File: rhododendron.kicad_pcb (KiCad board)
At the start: 2 copper layers, 70.7 x 53.3 mm, 42 parts, among them J1 Conn_02x20_Odd_Even, J2 Conn_02x20_Odd_Even, J4 USB-A-SHIELDED, J5 USB-B-SHIELDED, J7 BONUS_ROW, U1 USB3343, Y1 26MHz

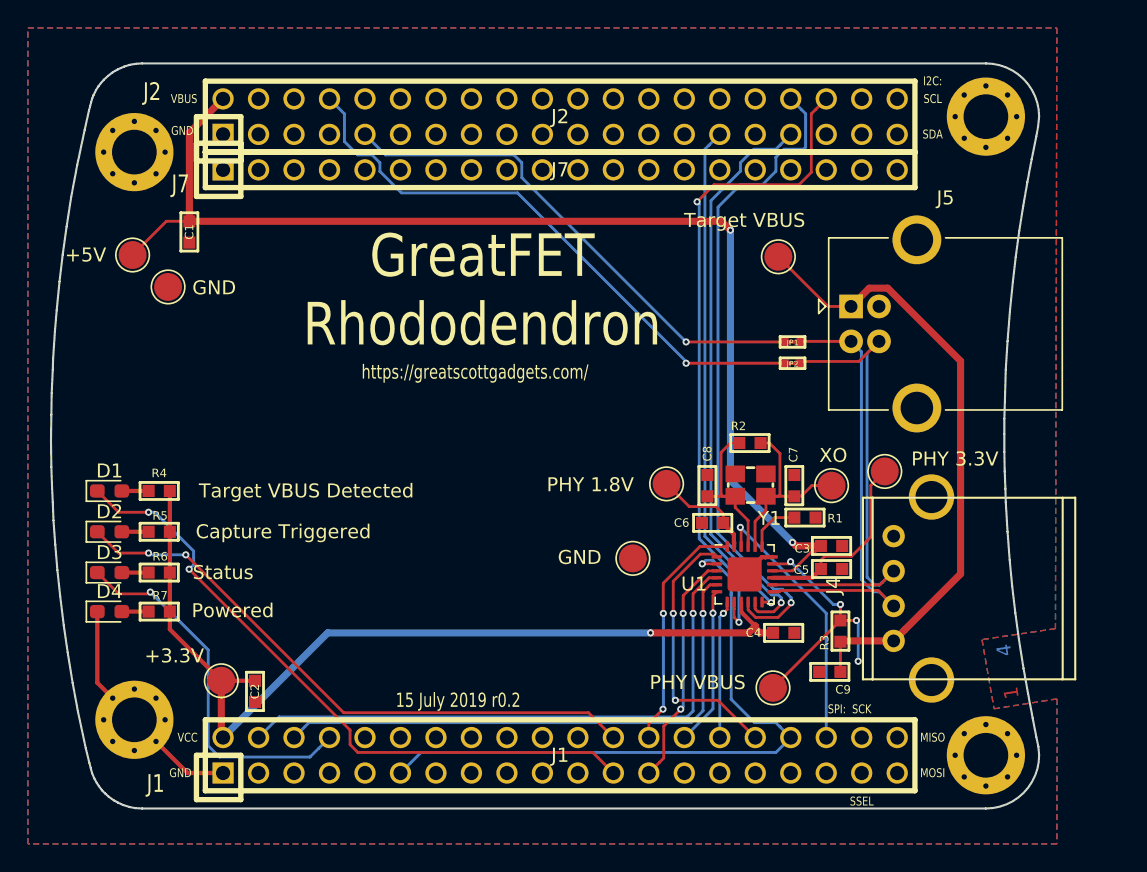
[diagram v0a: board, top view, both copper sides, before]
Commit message: r0.2: finalize for ordering; improve silkscreen; minor tweaks
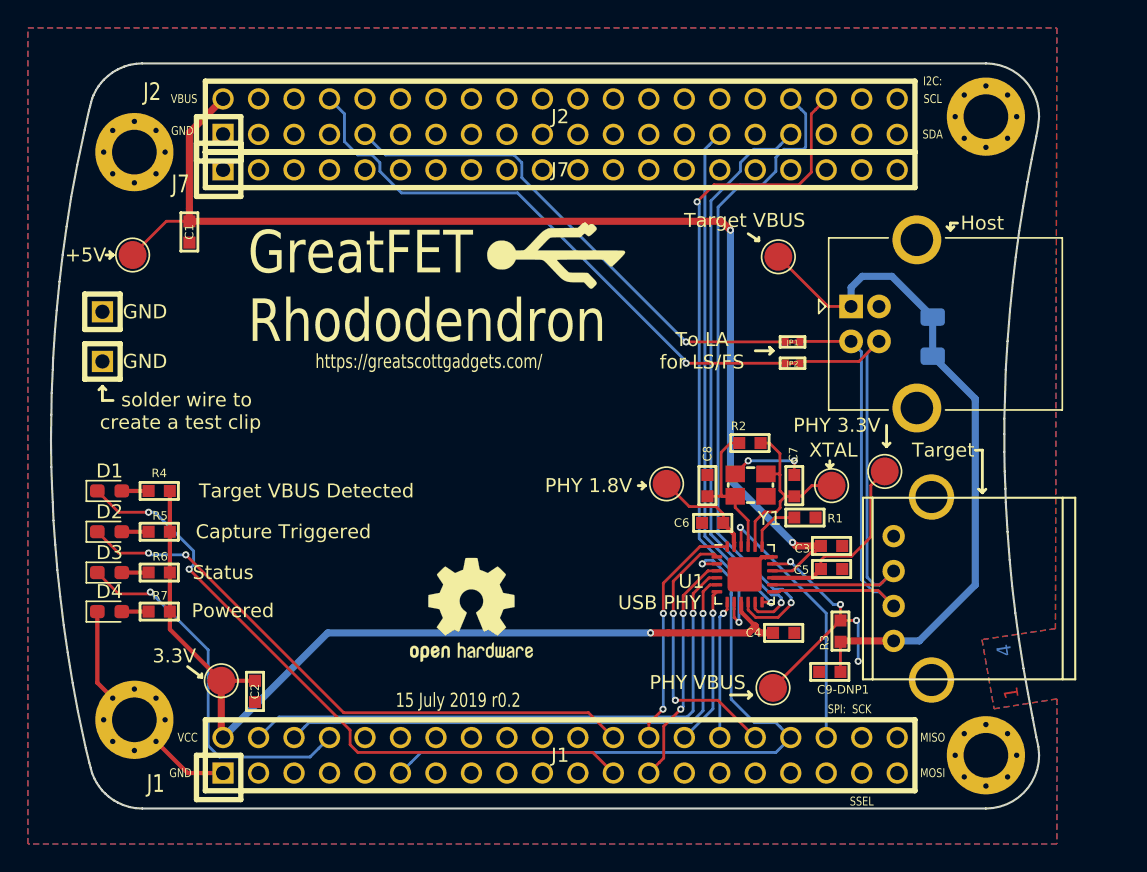
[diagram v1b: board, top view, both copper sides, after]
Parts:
- removed the GND at (118.0, 84.6)
- removed the GND at (151.3, 104.0)
- removed J4: USB-A-SHIELDED, rhododendron:CONN-Amphenol-UE27AC54100
- removed J5: USB-B-SHIELDED, rhododendron:USB_B_OST_USB-B1HSxx_Horizontal
- added G***: LOGO, rhododendron:usb_tools_logo, F.Cu at (145.8, 82.3)
- added G***: LOGO, rhododendron:usb_tools_logo, F.Cu at (142.2, 105.4)
- added GND: TestPoint, gsg-modules:HEADER-1x1, F.Cu at (113.3, 89.9)
- added GND: TestPoint, gsg-modules:HEADER-1x1, F.Cu at (113.3, 86.4)
- added Host: USB-B-SHIELDED, rhododendron:USB_B_OST_USB-B1HSxx_Horizontal, F.Cu at (166.9, 86.0)
- added R8: DNP, Resistor_SMD:R_1206_3216Metric, B.Cu at (172.7, 88.1)
- added REF**: OSHW-Logo2_9.8x8mm_SilkScreen, Symbol:OSHW-Logo2_9.8x8mm_SilkScreen, F.Cu at (139.7, 107.7)
- added Target: USB-A-SHIELDED, rhododendron:CONN-Amphenol-UE27AC54100, F.Cu at (169.9, 106.2)
- renumbered +3.3V to 3.3V, C9 to C9-DNP1, XO to XTAL
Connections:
- net /PHY_26MHZ_IN renamed /PHY_XI
- Y1 pad 2: /PHY_XO -> GND
- Y1 pad 3: (no net) -> /PHY_XO
- Y1 pad 4: (no net) -> GND
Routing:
- net GND: track 19.3 -> 25.8 mm, vias 0 -> 2
- net /TARGET_VBUS: track 45.2 -> 49.4 mm
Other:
- board text added: "To LA for LS/FS"
- board text added: "USB PHY"
- board text added: "cut trace to separate VBUSes or add a current-sense resistor"
- board text added: "solder wire to create a test clip"

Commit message: r0.3: route the changes made in the r0.3 schematic
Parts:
- removed C8: 8.2pF, gsg-modules:0603
- removed PHY VBUS: TestPoint, TestPoint:TestPoint_Pad_D2.0mm
- removed XTAL: TestPoint, TestPoint:TestPoint_Pad_D2.0mm
- removed Y1: 26MHz, gsg-modules:XTAL3.2x2.5mm
- added D5: LED, LED_SMD:LED_0603_1608Metric_Pad1.05x0.95mm_HandSolder, F.Cu at (113.7, 108.5)
- added JP3: Jumper_NC_Small, gsg-modules:0402-SHORT-10MIL, F.Cu at (146.6, 83.9)
- added R10: 1K, gsg-modules:0603, F.Cu at (162.7, 90.0)
- added R12: 1K, gsg-modules:0603, F.Cu at (165.1, 79.6)
- added R13: 1K5, gsg-modules:0603, F.Cu at (168.3, 79.6)
- added R14: 10K, gsg-modules:0603, F.Cu at (167.3, 114.3)
- added R9: 1K, gsg-modules:0603, F.Cu at (162.7, 88.5)
- added TP4: TestPoint, TestPoint:TestPoint_Pad_D2.0mm, F.Cu at (156.6, 97.0)
- added TP6: TestPoint, TestPoint:TestPoint_Pad_D2.0mm, F.Cu at (161.3, 113.3)
- added TP7: TestPoint, TestPoint:TestPoint_Pad_D2.0mm, F.Cu at (141.6, 82.3)
- added U2: M24C02-FMN, Package_SO:SOIC-8_3.9x4.9mm_P1.27mm, F.Cu at (151.5, 83.3)
- C7: value 8.2pF -> 10nF
- R2: value 1M -> 330
- TP1: renamed from PHY 3.3V
- TP5: renamed from PHY 1.8V
- TP8: renamed from Target VBUS
- moved R2 44.3 mm to (117.2, 108.5), turned to 0 degrees
- moved JP2 17.7 mm to (146.6, 82.7)
- moved JP1 17.7 mm to (146.5, 81.4)
- moved C7 16.6 mm to (151.3, 86.9), turned to 0 degrees
- moved G*** 10.4 mm to (151.1, 91.2)
- moved TP1 3.51 mm to (165.9, 98.6)
- moved REF** 2.96 mm to (140.2, 104.8)
- moved D2 2.42 mm to (113.7, 99.7)
- moved R5 2.42 mm to (117.2, 99.7)
- moved D1 2.42 mm to (113.7, 96.8)
- moved D3 2.42 mm to (113.7, 102.6)
- moved D4 2.42 mm to (113.7, 105.4)
- moved R4 2.42 mm to (117.2, 96.8)
- moved R6 2.42 mm to (117.2, 102.6)
- moved R7 2.42 mm to (117.2, 105.4)
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- renumbered C9-DNP1 to C9, Target to Device, +5V to TP2, 3.3V to TP3, GND to TP9
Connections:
- net /LED_STATUS renamed /LED_CAPTURING
- C7 pad 2: /PHY_XO -> +3V3
- J1 pad 11: /ULPI_CLK -> +3V3
- J1 pad 14: /P5_2 -> /LED_ERROR
- J1 pad 16: /P1_6 -> /ULPI_DIR
- J1 pad 34: /ULPI_CLK -> +3V3
- J1 pad 35: /P2_0 -> /~PHY_RESET
- J1 pad 36: /~PHY_RESET -> /P6_3
- J1 pad 7: /P1_0 -> /ULPI_NXT
- J2 pad 12: /CLK2 -> /REFCLK
- J2 pad 18: /P2_5 -> /REFCLK
- J2 pad 20: /P2_3 -> /ULPI_DATA5
- J2 pad 23: /P7_2 -> /ULPI_DATA4
- J2 pad 37: /P3_5 -> /TARGET_VBUS_DETECT
- J2 pad 38: /P3_6 -> /I2C_EEPROM_WC
- J7 pad 10: GND -> /RTCX1
- J7 pad 20: VCC -> +3V3
- J7 pad 4: /ADC0_5 -> /PHY_VDD18
- JP1 pad 1: /LA_USB_D- -> GND
- JP1 pad 2: /USB_D- -> Net-(JP1-Pad2)
- JP2 pad 1: /LA_USB_D+ -> GND
- JP2 pad 2: /USB_D+ -> Net-(JP2-Pad2)
- R2 pad 1: /PHY_XO -> Net-(D5-Pad2)
- R2 pad 2: /PHY_XI -> +3V3
- U1 pad 2: /ULPI_CLK -> +3V3
- U1 pad 20: /PHY_XO -> Net-(U1-Pad20)
- U1 pad 21: /PHY_XI -> /REFCLK
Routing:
- net +3V3: track 66.8 -> 132.2 mm, vias 1 -> 11
- net /REFCLK: track 0.00 -> 53.3 mm, vias 0 -> 1
- net /ULPI_CLK: track 46.9 -> 0.00 mm, vias 1 -> 0
- net /PHY_VDD18: track 7.61 -> 49.7 mm, vias 0 -> 1
- net /LED_ERROR: track 0.00 -> 31.7 mm
- net /ULPI_NXT: track 16.9 -> 40.8 mm
- net /I2C0_SCL: track 0.00 -> 23.4 mm
- net /I2C0_SDA: track 0.00 -> 21.9 mm
- net /I2C_EEPROM_WC: track 0.00 -> 21.0 mm, vias 0 -> 1
- net /ULPI_DATA5: track 47.8 -> 66.7 mm
- net /ULPI_DIR: track 19.4 -> 36.2 mm
- net /ULPI_DATA4: track 47.8 -> 62.8 mm
- net /PHY_XO: track 14.6 -> 0.00 mm
- net /PHY_XI: track 11.6 -> 0.00 mm
- net GND: track 25.8 -> 16.0 mm
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- added copper zone on B.Cu, net +3V3
- removed copper zone on B.Cu, net VCC
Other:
- board size 70.7 x 53.3 mm -> 73.7 x 53.3 mm
- board text added: "16 October 2019 r0.3"
- board text added: "2"
- board text added: "3.3V"
- board text added: "5V"
- board text added: "Capture Active"
- board text added: "Error"
- board text added: "GND Clip"
- board text added: "High Speed USB Analyzer for GreatFET"
- board text added: "ID ROM"
- board text added: "PHY 1.8V"
- board text added: "PHY 3.3V"
- board text added: "PHY Clock"
- board text added: "PHY VBus"
- board text added: "Rhododendron"
- board text added: "VCCIO 3.3V"
- board text added: "design by Kate Temkin (@ktemkin); with help from Mikaela Szekely (@Qyriad)"
- board text removed: "15 July 2019 r0.2"
- board text removed: "4"
- board text removed: "GreatFET Rhododendron"
- board text removed: "MISO"
- board text removed: "MOSI"
- board text removed: "SCK"
- board text removed: "SPI:"
- board text removed: "SSEL"
- board text removed: "Status"
- board text removed: "To LA for LS/FS"
- board text removed: "design by @ktemkin; with help from @Qyriad"
- board text removed: "solder wire to create a test clip"

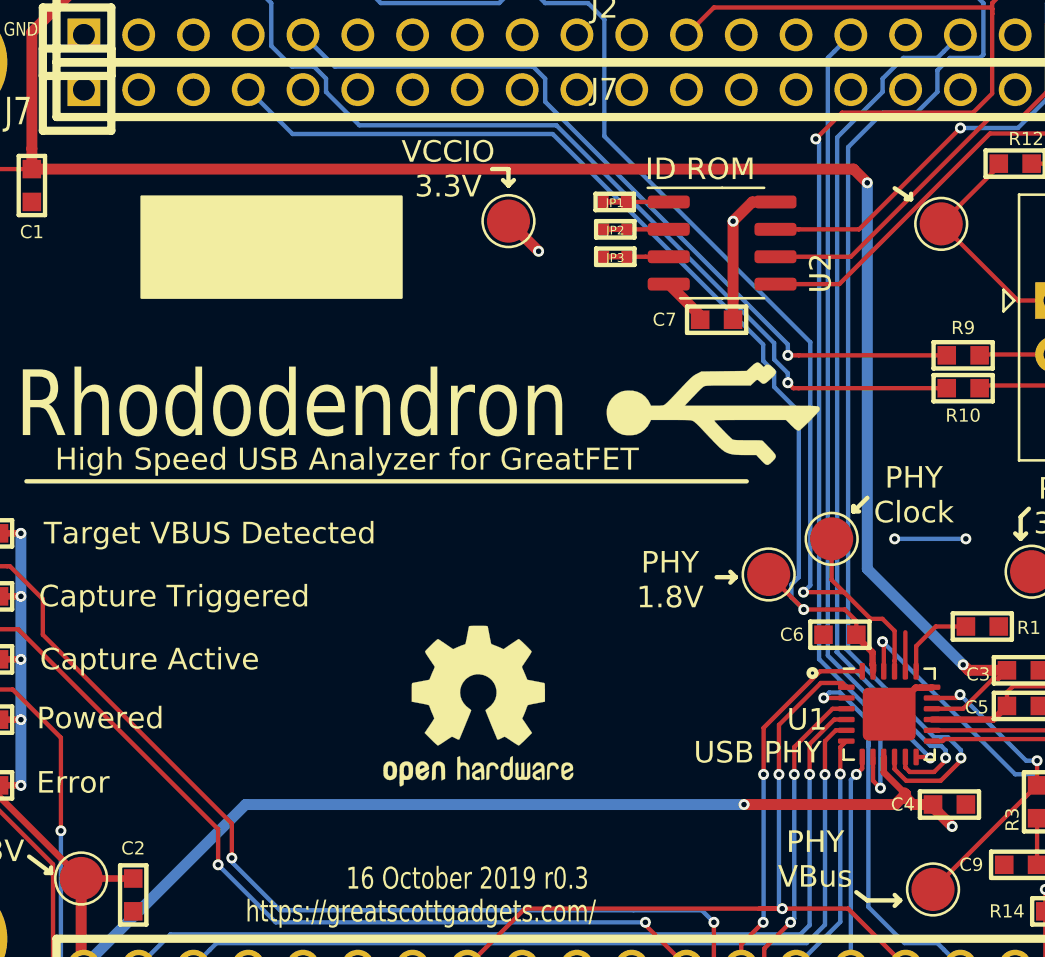
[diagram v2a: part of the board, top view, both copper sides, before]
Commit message: r0.3: add 3d models and prepare for plotting
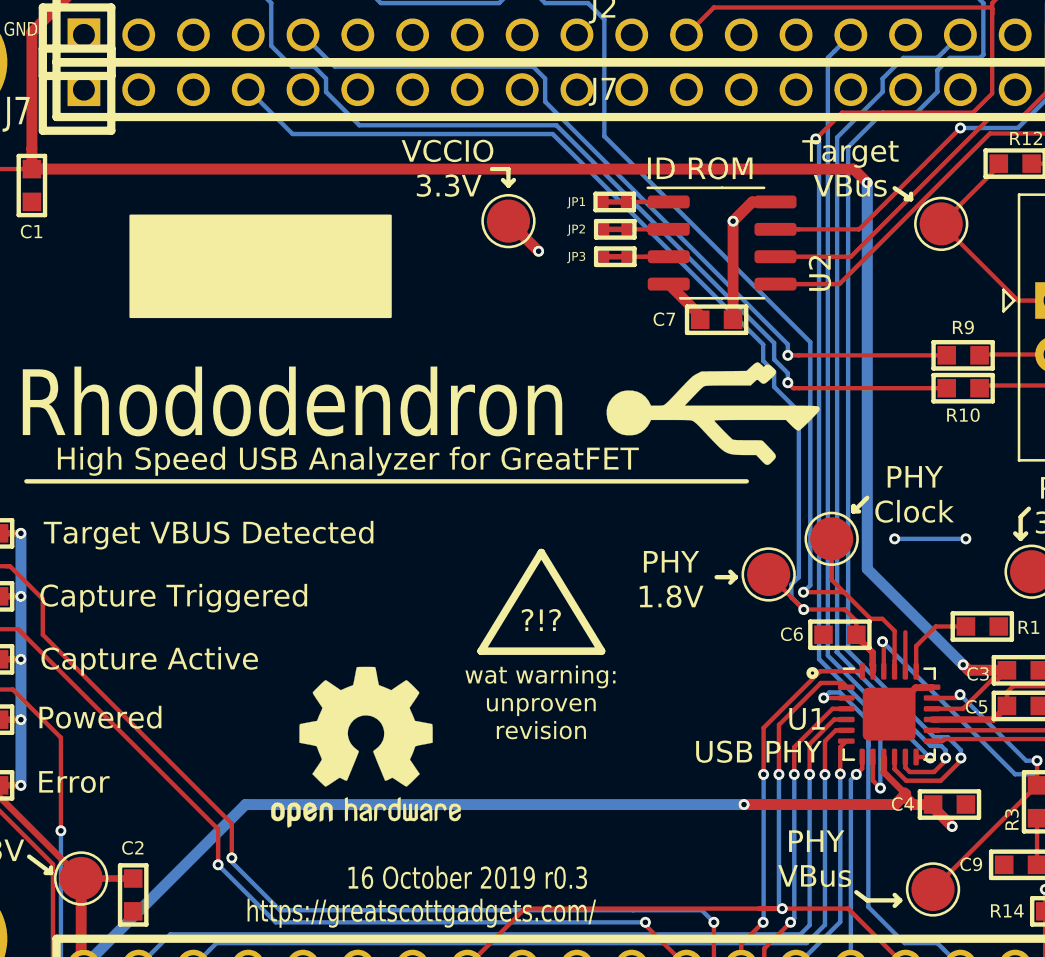
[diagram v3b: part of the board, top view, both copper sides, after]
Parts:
- added REF**: WEEE-Logo_8.4x12mm_SilkScreen, Symbol:WEEE-Logo_8.4x12mm_SilkScreen, B.Cu at (118.6, 99.7)
- added REF**: ESD-Logo_8.9x8mm_SilkScreen, Symbol:ESD-Logo_8.9x8mm_SilkScreen, B.Cu at (130.4, 98.7)
- moved REF** 5.54 mm to (135.0, 106.7)
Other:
- board text added: "?!?"
- board text added: "DO NOT PINCH"
- board text added: "HOPEFULLY NOT TRASH"
- board text added: "Target VBus"
- board text added: "wat warning: unproven revision"
